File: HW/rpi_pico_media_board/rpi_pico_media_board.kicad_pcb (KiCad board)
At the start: 4 copper layers, 100 x 80 mm, 137 parts, among them J1 Barrel_Jack_Switch_Pin3Ring, J200 Conn_01x04_Pin, J201 Conn_01x03, J300 AudioJack3_Ground_SwitchTR, J301 Conn_01x03_Pin, J400 TF-01A, Q100 T2N7002AK, Q500 T2N7002AK, Q501 T2N7002AK, Q502 T2N7002AK, SW200 SW_DPDT_XLX, U100 HT7533-1, U101 HT7533-1, U200 RaspberryPi_Pico, U202 mems-mic, U203 mems-mic, U300 PCM5102A, U500 SW, U501 SW, U502 SW, U503 SW, U504 SW, U505 SW, U506 SW, U507 SW, U508 SW, U509 SW, U510 SW, U511 SW, U600 PCF8563TS, Y600 32768Hz

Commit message: Macro Pad routing
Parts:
- moved R108 7.85 mm to (138.8, 94.8)
- moved R107 7.66 mm to (146.5, 94.8), turned to 90 degrees
- moved C500 7.00 mm to (99.8, 79.5)
- moved C502 7.00 mm to (99.8, 86.5)
- moved R504 7.00 mm to (99.8, 81.2)
- moved R506 7.00 mm to (99.8, 88.2)
- moved D601 5.54 mm to (145.8, 79.2), turned to -90 degrees
- moved D600 4.96 mm to (145.8, 74.0), turned to 90 degrees
- moved C601 3.91 mm to (148.0, 80.0)
- moved C600 3.91 mm to (148.0, 76.8)
- moved C101 2.50 mm to (115.2, 63.2)
- moved D508 2.30 mm to (112.8, 125.8), turned to 0 degrees
- moved D509 2.30 mm to (122.8, 125.8), turned to 0 degrees
- moved D510 2.30 mm to (132.8, 125.8), turned to 0 degrees
- moved D511 2.30 mm to (142.8, 125.8), turned to 0 degrees
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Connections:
- U200 pad 26: MACRO_PAD_BTN_ROW_0 -> MACRO_PAD_BTN_ROW_2
- U200 pad 29: MACRO_PAD_BTN_ROW_2 -> MACRO_PAD_BTN_ROW_0
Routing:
- net Net-(R500-Pad2): track 0.00 -> 126.2 mm, vias 0 -> 1
- net Net-(R501-Pad2): track 0.00 -> 114.3 mm, vias 0 -> 1
- net Net-(R502-Pad2): track 0.00 -> 99.9 mm, vias 0 -> 1
- net PG_3V3: track 0.00 -> 98.1 mm
- net Net-(R503-Pad2): track 0.00 -> 87.4 mm, vias 0 -> 1
- net Net-(D508-K): track 0.00 -> 81.0 mm
- net Net-(D504-K): track 0.00 -> 74.7 mm
- net Net-(D500-K): track 0.00 -> 68.1 mm
- net USR_LED_2: track 0.00 -> 52.7 mm
- net USR_LED_1: track 0.00 -> 38.9 mm
- net +5V: track 0.00 -> 31.6 mm
- net +RPI_VBUS: track 0.00 -> 30.8 mm
- net USR_LED_0: track 0.00 -> 28.5 mm
- net +3.3V: track 0.00 -> 18.2 mm, vias 0 -> 1
- net VCC: track 0.00 -> 16.6 mm
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- added copper zone on In1.Cu, net GND
- added copper zone on In2.Cu, net GND

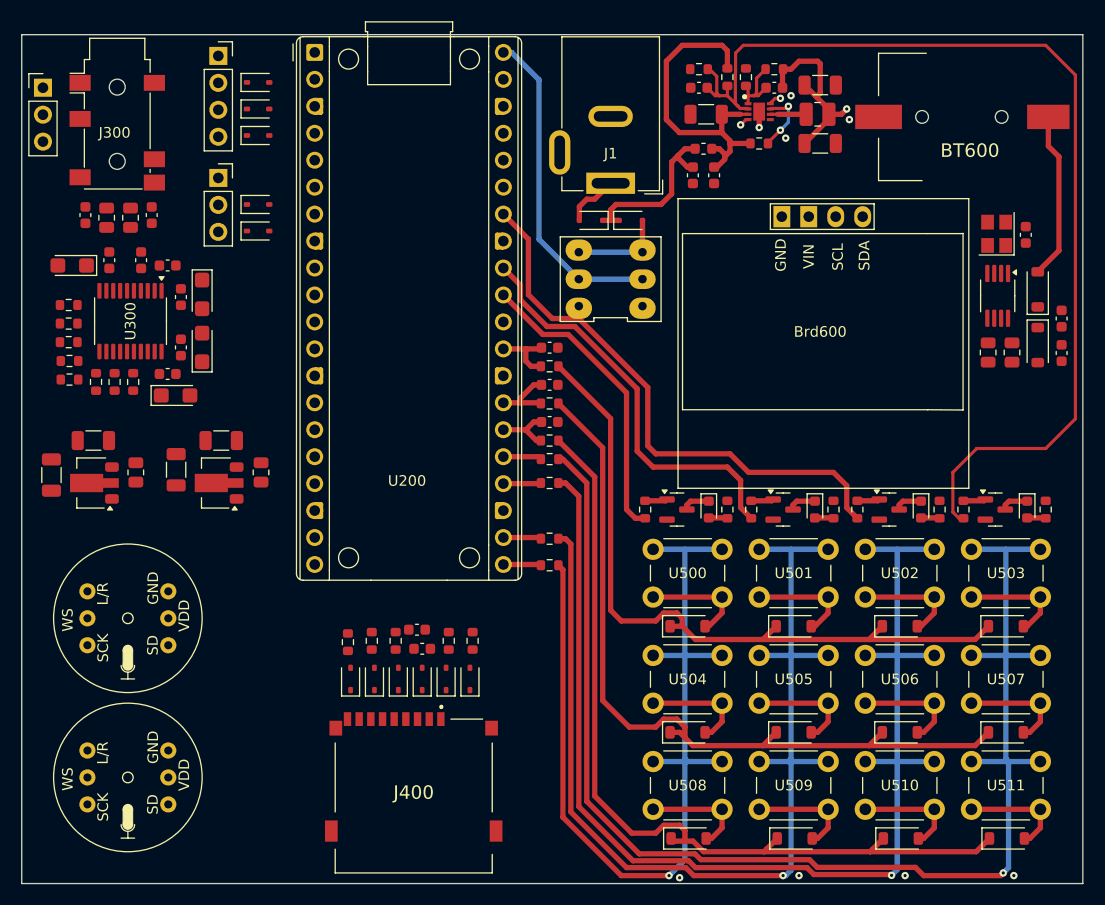
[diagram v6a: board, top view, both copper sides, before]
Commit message: SD Card routing
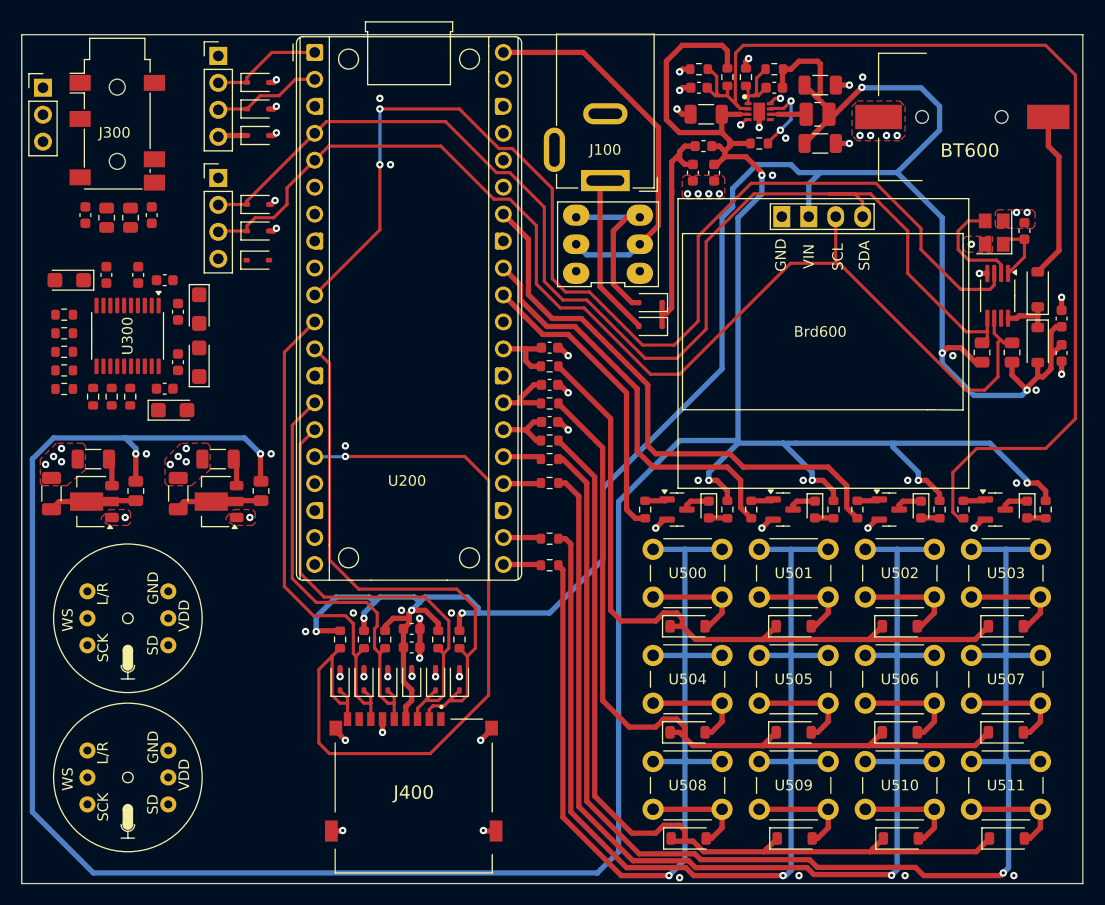
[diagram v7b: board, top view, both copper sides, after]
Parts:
- removed J1: Barrel_Jack_Switch_Pin3Ring, Connector_BarrelJack:BarrelJack_GCT_DCJ200-10-A_Horizontal
- added D4: PESD3V3L1BA,115, Diode_SMD:D_SOD-323, F.Cu at (72.2, 71.2)
- added J100: Barrel_Jack_Switch_Pin3Ring, Connector_BarrelJack:BarrelJack_GCT_DCJ200-10-A_Horizontal, F.Cu at (105.0, 63.8)
- J200: footprint Connector_PinSocket_2.54mm:PinSocket_1x04_P2.54mm_Vertical -> Connector_PinHeader_2.54mm:PinHeader_1x04_P2.54mm_Vertical
- J201: value Conn_01x03 -> Conn_01x04_Pin; footprint Connector_PinSocket_2.54mm:PinSocket_1x03_P2.54mm_Vertical -> Connector_PinHeader_2.54mm:PinHeader_1x04_P2.54mm_Vertical
- moved D100 11.5 mm to (109.2, 77.5)
- moved D200 7.97 mm to (109.2, 75.2), turned to 180 degrees
- moved SW200 3.30 mm to (105.2, 69.8)
- moved C107 2.26 mm to (64.8, 93.2)
- moved C108 1.78 mm to (68.5, 90.0)
- moved C109 1.75 mm to (52.8, 93.2)
- moved C110 1.75 mm to (56.8, 90.0)
- moved R105 1.75 mm to (72.5, 93.0)
- moved R106 1.75 mm to (60.8, 93.0)
- moved U100 1.75 mm to (68.3, 94.0)
- moved U101 1.75 mm to (56.5, 94.0)
- moved C303 1.41 mm to (64.2, 85.4)
- moved C304 1.41 mm to (64.7, 76.1)
- moved C305 1.41 mm to (66.7, 75.9)
- moved C306 1.41 mm to (64.7, 80.9)
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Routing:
- net +5V: track 31.6 -> 285.4 mm, vias 0 -> 7
- net +3.3V: track 18.2 -> 208.7 mm, vias 1 -> 7
- net I2C1_SDA: track 0.00 -> 115.6 mm
- net I2C1_SCL: track 0.00 -> 111.4 mm
- net PCF8563_INT: track 0.00 -> 109.8 mm, vias 0 -> 2
- net SPI1_SD_CARD_CARD_DETECT: track 0.00 -> 74.5 mm, vias 0 -> 1
- net SPI1_SD_CARD_CS: track 0.00 -> 52.1 mm
- net SPI1_SD_CARD_MISO: track 0.00 -> 46.7 mm
- net SPI1_SD_CARD_MOSI: track 0.00 -> 43.1 mm
- net SPI1_SD_CARD_SCK: track 0.00 -> 40.2 mm
- net GND: track 3.59 -> 42.6 mm, vias 10 -> 80
- net UART0_TX: track 0.00 -> 10.6 mm
- net VDC: track 5.16 -> 15.5 mm
- net UART0_RX: track 0.00 -> 10.3 mm
- net /[6]I2C_Peripherals/OSCO: track 0.00 -> 10.2 mm
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- added copper zone on F.Cu, net GND

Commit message: Initial PCB version
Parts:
- moved C311 6.75 mm to (62.8, 67.2)
- moved C310 5.76 mm to (56.5, 67.2)
- moved R303 5.17 mm to (53.2, 83.2)
- moved R306 3.71 mm to (53.2, 78.0)
- moved R307 3.71 mm to (53.2, 79.8)
- moved R304 1.78 mm to (53.2, 81.5)
- moved R301 0.81 mm to (58.5, 84.9)
- moved R300 0.81 mm to (60.2, 84.9)
- moved R302 0.81 mm to (56.7, 84.9)
- moved R305 0.76 mm to (53.2, 76.2)
- moved J300 0.50 mm to (59.5, 54.2)
- moved J301 0.50 mm to (52.5, 55.0)
- moved R308 0.50 mm to (58.5, 67.2)
- moved R309 0.50 mm to (60.8, 67.2)
- moved C306 0.36 mm to (64.8, 80.5)
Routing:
- net +3.3V: track 208.7 -> 368.0 mm, vias 7 -> 10
- net I2S_INMP441_SCL: track 0.00 -> 72.2 mm, vias 0 -> 1
- net I2S_INMP441_SCK: track 0.00 -> 65.9 mm, vias 0 -> 1
- net +3.3VA_INMP: track 2.61 -> 52.3 mm
- net I2S_INMP441_DATA: track 0.00 -> 41.4 mm, vias 0 -> 1
- net I2S_PCM5102_SCK: track 0.00 -> 37.4 mm
- net I2S_PCM5102_DATA: track 0.00 -> 37.1 mm
- net +3.3VA_PCM: track 3.04 -> 33.0 mm, vias 0 -> 2
- net I2S_PCM5102_SCL: track 0.00 -> 28.5 mm, vias 0 -> 1
- net GND: track 42.6 -> 63.3 mm, vias 80 -> 123
- net /[3]PCM5102/OUT_L: track 0.00 -> 20.5 mm
- net /[3]PCM5102/OUT_R: track 0.00 -> 15.9 mm
- net /[3]PCM5102/XSMT: track 0.00 -> 14.7 mm, vias 0 -> 2
- net /[3]PCM5102/FMT: track 0.00 -> 10.4 mm, vias 0 -> 2
- net /[3]PCM5102/OUTL: track 0.00 -> 7.82 mm
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- added copper zone on B.Cu, net GND
